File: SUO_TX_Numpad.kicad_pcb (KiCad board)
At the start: 2 copper layers, 78.5 x 124.6 mm, 95 parts, among them J1 USB_C_Receptacle_USB2.0_16P, SW1 BOOT, U1 STM32F411CEUx, U2 XC6206PxxxMR-Regulator_Linear, U3 USBLC6-2SC6, Y1 XTAL OSC XO 8.0000MHZ HCMOS S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

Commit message: Pulled A10 to ground; found that a BlackPill dev board wo'nt DFU properly without it. Updated SK6812MINI-E footprint to be a rotated one; track layout stays the same, but the old footprint was incorrect, resulting in all key LEDs shorting out
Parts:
- LED1, LED10, LED11, LED12, LED13, LED14, LED15, LED16, LED17, LED18, LED19, LED2, LED20, LED21, LED22, LED3, LED4, LED5, LED6, LED7, LED8, LED9: footprint kicad-keyboard-parts:MX_SK6812MINI-E_REV -> kicad-keyboard-parts:MX_SK6812MINI-E_REV_ROTATED
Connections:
- LED1 pad 1: GND -> VBUS
- LED1 pad 2: LED_DATA -> Net-(LED1-DOUT)
- LED1 pad 3: VBUS -> GND
- LED1 pad 4: Net-(LED1-DOUT) -> LED_DATA
- LED10 pad 1: GND -> VBUS
- LED10 pad 2: Net-(LED10-DIN) -> Net-(LED10-DOUT)
- LED10 pad 3: VBUS -> GND
- LED10 pad 4: Net-(LED10-DOUT) -> Net-(LED10-DIN)
- LED11 pad 1: GND -> VBUS
- LED11 pad 2: Net-(LED10-DOUT) -> Net-(LED11-DOUT)
- LED11 pad 3: VBUS -> GND
- LED11 pad 4: Net-(LED11-DOUT) -> Net-(LED10-DOUT)
- LED12 pad 1: GND -> VBUS
- LED12 pad 2: Net-(LED11-DOUT) -> Net-(LED12-DOUT)
- LED12 pad 3: VBUS -> GND
- LED12 pad 4: Net-(LED12-DOUT) -> Net-(LED11-DOUT)
- LED13 pad 1: GND -> VBUS
- LED13 pad 2: Net-(LED12-DOUT) -> Net-(LED13-DOUT)
- LED13 pad 3: VBUS -> GND
- LED13 pad 4: Net-(LED13-DOUT) -> Net-(LED12-DOUT)
- LED14 pad 1: GND -> VBUS
- LED14 pad 2: Net-(LED13-DOUT) -> Net-(LED14-DOUT)
- LED14 pad 3: VBUS -> GND
- LED14 pad 4: Net-(LED14-DOUT) -> Net-(LED13-DOUT)
- LED15 pad 1: GND -> VBUS
- LED15 pad 2: Net-(LED14-DOUT) -> Net-(LED15-DOUT)
- LED15 pad 3: VBUS -> GND
- LED15 pad 4: Net-(LED15-DOUT) -> Net-(LED14-DOUT)
- LED16 pad 1: GND -> VBUS
- LED16 pad 2: Net-(LED15-DOUT) -> Net-(LED16-DOUT)
- LED16 pad 3: VBUS -> GND
- LED16 pad 4: Net-(LED16-DOUT) -> Net-(LED15-DOUT)
- LED17 pad 1: GND -> VBUS
- LED17 pad 2: Net-(LED16-DOUT) -> Net-(LED17-DOUT)
- LED17 pad 3: VBUS -> GND
- LED17 pad 4: Net-(LED17-DOUT) -> Net-(LED16-DOUT)
- LED18 pad 1: GND -> VBUS
- LED18 pad 2: Net-(LED17-DOUT) -> Net-(LED18-DOUT)
- LED18 pad 3: VBUS -> GND
- LED18 pad 4: Net-(LED18-DOUT) -> Net-(LED17-DOUT)
- LED19 pad 1: GND -> VBUS
- LED19 pad 2: Net-(LED18-DOUT) -> Net-(LED19-DOUT)
- LED19 pad 3: VBUS -> GND
- LED19 pad 4: Net-(LED19-DOUT) -> Net-(LED18-DOUT)
- LED2 pad 1: GND -> VBUS
- LED2 pad 2: Net-(LED1-DOUT) -> Net-(LED2-DOUT)
- LED2 pad 3: VBUS -> GND
- LED2 pad 4: Net-(LED2-DOUT) -> Net-(LED1-DOUT)
- LED20 pad 1: GND -> VBUS
- LED20 pad 2: Net-(LED19-DOUT) -> Net-(LED20-DOUT)
- LED20 pad 3: VBUS -> GND
- LED20 pad 4: Net-(LED20-DOUT) -> Net-(LED19-DOUT)
- LED21 pad 1: GND -> VBUS
- LED21 pad 2: Net-(LED20-DOUT) -> LED_TO_UNDER
- LED21 pad 3: VBUS -> GND
- LED21 pad 4: LED_TO_UNDER -> Net-(LED20-DOUT)
- LED22 pad 1: GND -> VBUS
- LED22 pad 2: LED_TO_STATUS -> unconnected-(LED22-DOUT-Pad2)
- LED22 pad 3: VBUS -> GND
- LED22 pad 4: unconnected-(LED22-DOUT-Pad4) -> LED_TO_STATUS
- LED3 pad 1: GND -> VBUS
- LED3 pad 2: Net-(LED2-DOUT) -> Net-(LED3-DOUT)
- LED3 pad 3: VBUS -> GND
- LED3 pad 4: Net-(LED3-DOUT) -> Net-(LED2-DOUT)
- LED4 pad 1: GND -> VBUS
- LED4 pad 2: Net-(LED3-DOUT) -> Net-(LED4-DOUT)
- LED4 pad 3: VBUS -> GND
- LED4 pad 4: Net-(LED4-DOUT) -> Net-(LED3-DOUT)
- LED5 pad 1: GND -> VBUS
- LED5 pad 2: Net-(LED4-DOUT) -> Net-(LED5-DOUT)
- LED5 pad 3: VBUS -> GND
- LED5 pad 4: Net-(LED5-DOUT) -> Net-(LED4-DOUT)
- LED6 pad 1: GND -> VBUS
- LED6 pad 2: Net-(LED5-DOUT) -> Net-(LED6-DOUT)
- LED6 pad 3: VBUS -> GND
- LED6 pad 4: Net-(LED6-DOUT) -> Net-(LED5-DOUT)
- LED7 pad 1: GND -> VBUS
- LED7 pad 2: Net-(LED6-DOUT) -> Net-(LED7-DOUT)
- LED7 pad 3: VBUS -> GND
- LED7 pad 4: Net-(LED7-DOUT) -> Net-(LED6-DOUT)
- LED8 pad 1: GND -> VBUS
- LED8 pad 2: Net-(LED7-DOUT) -> Net-(LED8-DOUT)
- LED8 pad 3: VBUS -> GND
- LED8 pad 4: Net-(LED8-DOUT) -> Net-(LED7-DOUT)
- LED9 pad 1: GND -> VBUS
- LED9 pad 2: Net-(LED8-DOUT) -> Net-(LED10-DIN)
- LED9 pad 3: VBUS -> GND
- LED9 pad 4: Net-(LED10-DIN) -> Net-(LED8-DOUT)
- U1 pad 31: unconnected-(U1-PA10-Pad31) -> GND
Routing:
- net VBUS: track 622.7 -> 612.1 mm
- net GND: track 287.8 -> 295.7 mm
- net COL4: track 111.0 -> 105.4 mm
- net Net-(UNDER3-DOUT): track 26.3 -> 24.9 mm

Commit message: Added freqency marker for HCMOS XTAL
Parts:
- Y1: value XTAL OSC XO 8.0000MHZ HCMOS SMD -> XTAL OSC XO 25.0000MHZ HCMOS SMD
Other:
- board text added: "25MHz"
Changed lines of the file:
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@@
 		(property "Reference" "Y1"
 			(at 0 2.5 0)
-			(layer "B.SilkS")
+			(layer "B.Fab")
 			(effects
 				(font
@@
 			)
 		)
-		(property "Value" "XTAL OSC XO 8.0000MHZ HCMOS SMD"
+		(property "Value" "XTAL OSC XO 25.0000MHZ HCMOS SMD"
 			(at 0 -2.5 0)
 			(layer "B.Fab")
@@
 			)
 		)
-		(property "DigiKey" "1923-LFSPXO072801CT-ND"
+		(property "DigiKey" "XC2198CT-ND"
 			(at 0 0 180)
 			(unlocked yes)
@@
 		(layer "Edge.Cuts")
 	)
+	(gr_text "25MHz"
+		(at 155.755543 93.984351 270)
+		(layer "B.SilkS")
+		(effects
+			(font
+				(size 1.1 1.5)
+				(thickness 0.15)
+			)
+			(justify left bottom mirror)
+		)
+	)
 	(gr_text "U1: stm32f411ce\nU2: XC6206\nU3: USBLC6-2SC6"

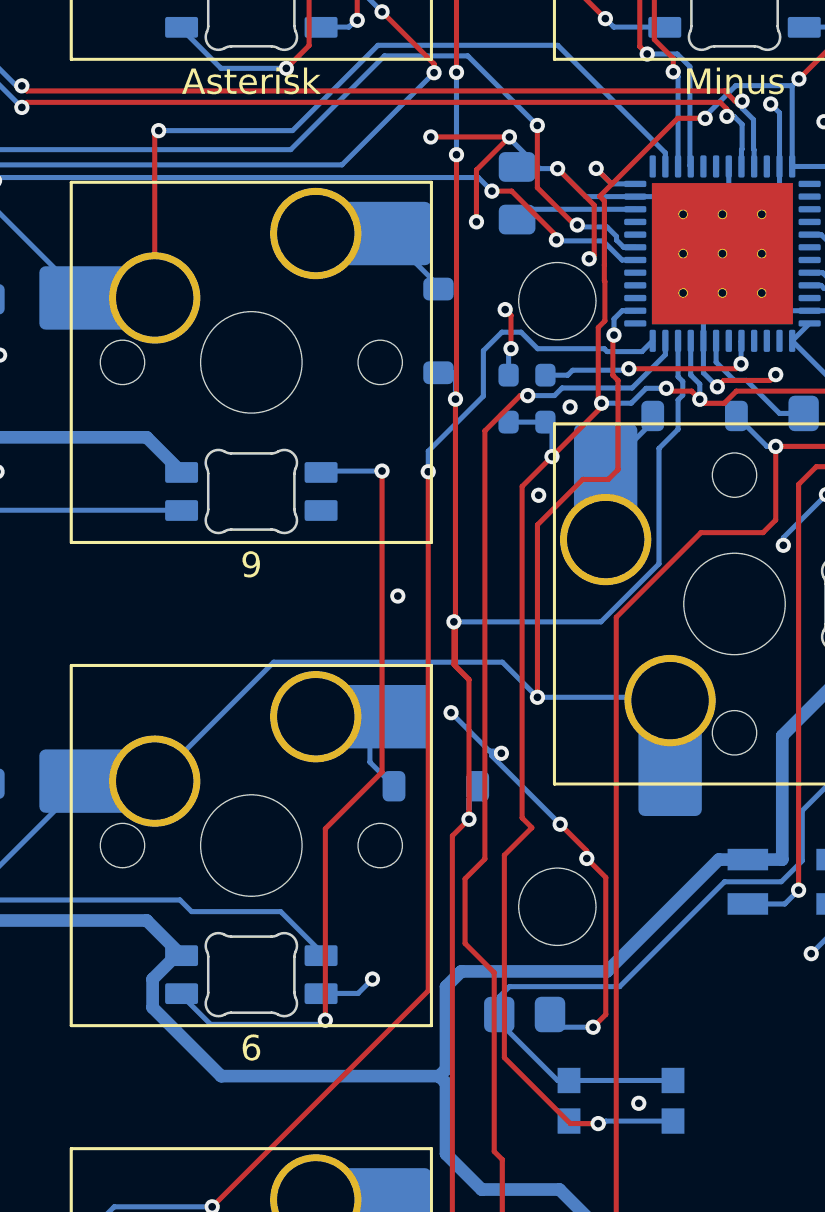
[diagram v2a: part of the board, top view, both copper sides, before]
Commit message: Added 3225 active oscillator, unsure if pin 1 is in fact enable, is in fact active high, so a jumper pad to pick either is added
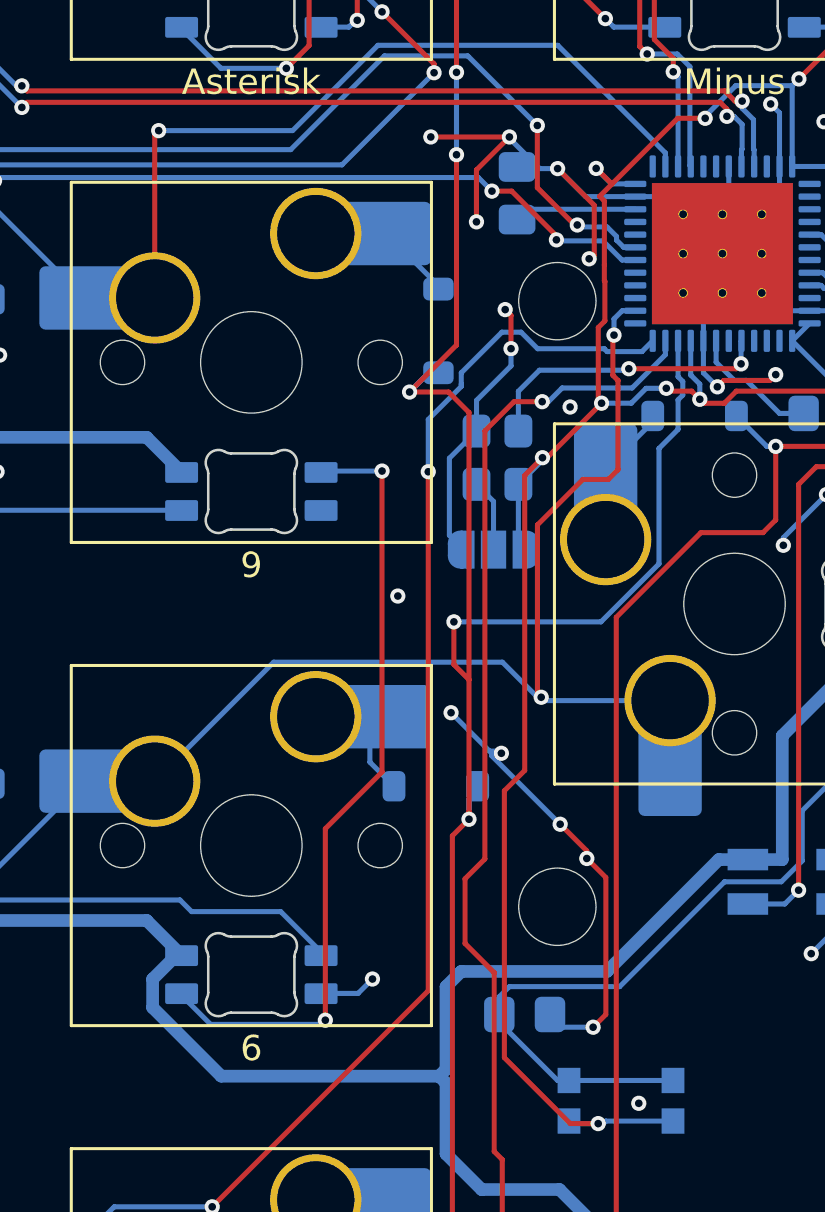
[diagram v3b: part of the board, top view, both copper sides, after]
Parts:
- added JP1: SolderJumper_3_Open, Jumper:SolderJumper-3_P1.3mm_Open_RoundedPad1.0x1.5mm, B.Cu at (157.2, 93.1)
- Y1: value XTAL OSC XO 25.0000MHZ HCMOS SMD -> ASE-xxxMHz; footprint Oscillator:Oscillator_SMD_ECS_2520MV-xxx-xx-4Pin_2.5x2.0mm -> Oscillator:Oscillator_SMD_Abracon_ASE-4Pin_3.2x2.5mm
- moved Y1 2.61 mm to (157.3, 89.5), turned to 90 degrees
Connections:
- net Net-(U1-PH0) renamed MCU_PH0
- U1 pad 6: unconnected-(U1-PH1-Pad6) -> MCU_PH1
- Y1 pad 1: +3V3 -> Net-(JP1-C)
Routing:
- net GND: track 295.7 -> 303.7 mm, vias 111 -> 110
- net MCU_PH0: track 8.81 -> 11.7 mm
- net Net-(JP1-C): track 0.00 -> 2.73 mm
- net COL3: track 129.0 -> 131.2 mm
- net +3V3: track 111.9 -> 113.5 mm

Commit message: Fixed wiring mistake on USBLC6-2SC6
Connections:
- U3 pad 1: USB_D- -> MCU_D+
- U3 pad 3: MCU_D+ -> MCU_D-
- U3 pad 4: MCU_D- -> USB_D-
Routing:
- net GND: track 303.7 -> 324.6 mm, vias 110 -> 165
- net VBUS: track 612.1 -> 616.5 mm
- net USB_D+: track 31.1 -> 27.1 mm
- net MCU_D+: track 51.5 -> 49.1 mm
- net MCU_D-: track 51.0 -> 49.2 mm
- net Net-(LED19-DOUT): track 15.2 -> 14.6 mm
- net USB_5V: track 22.7 -> 23.3 mm
